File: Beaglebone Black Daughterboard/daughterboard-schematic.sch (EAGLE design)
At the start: 6 parts

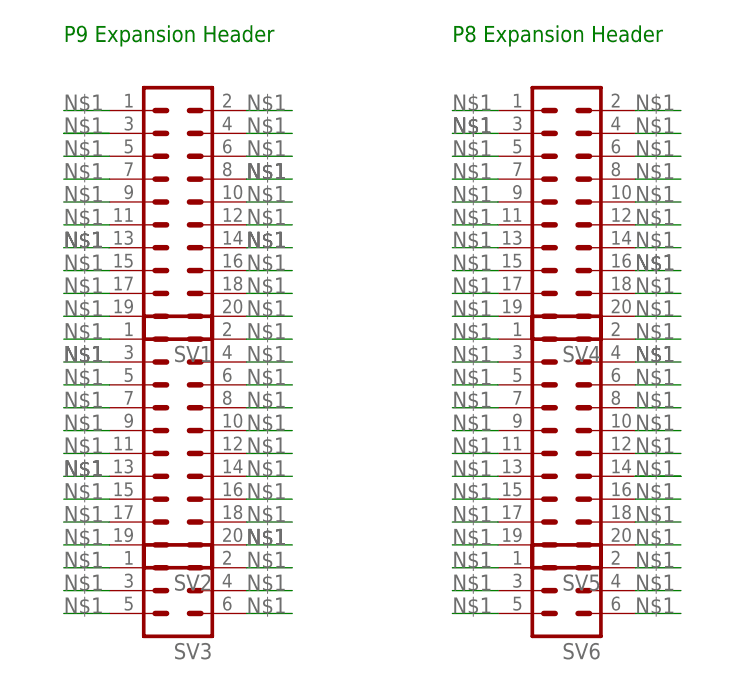
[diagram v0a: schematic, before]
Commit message: Label ports on Cape Expansion ready for wiring
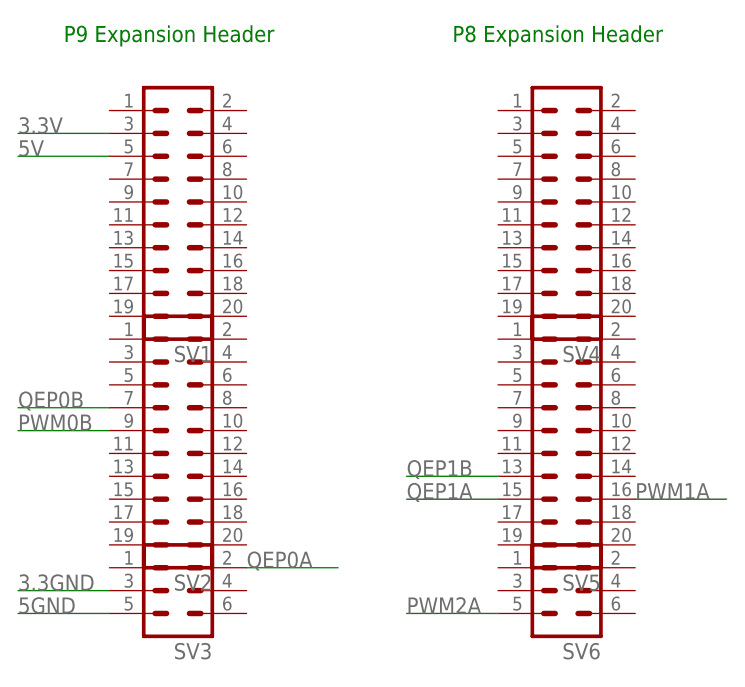
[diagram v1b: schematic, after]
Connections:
- net N$1 renamed 5V
- new net 3.3GND: SV3.3
- new net 3.3V: SV1.3
- new net 5GND: SV3.5
- new net PWM0B: SV2.9
- new net PWM1A: SV5.16
- new net PWM2A: SV6.5
- new net QEP0A: SV3.2
- new net QEP0B: SV2.7
- new net QEP1A: SV5.15
- new net QEP1B: SV5.13

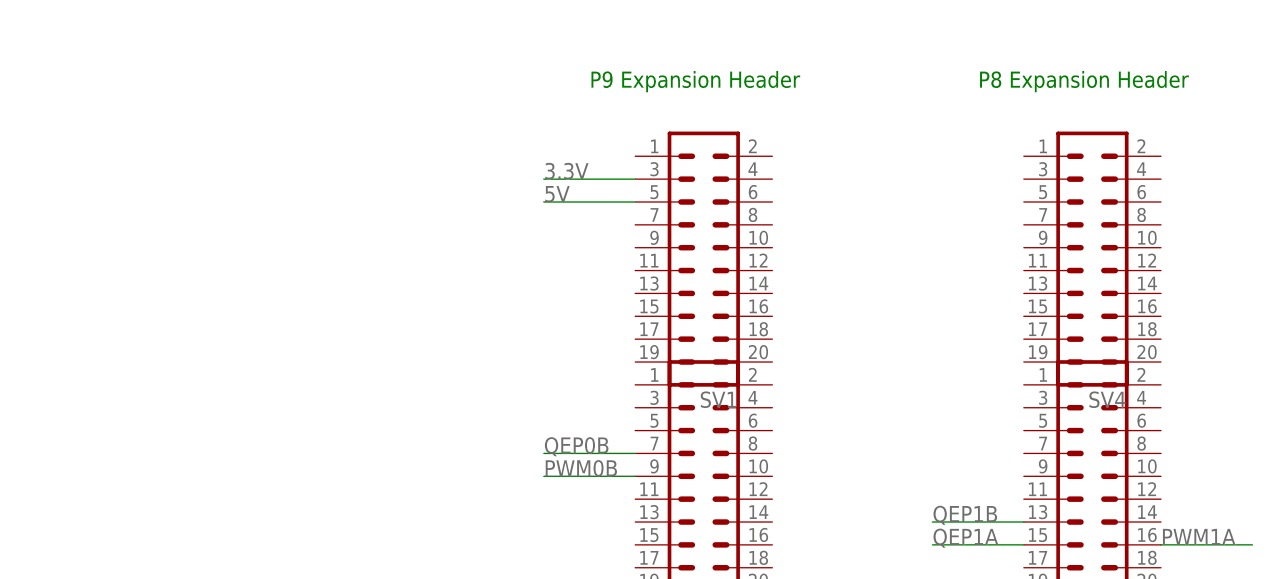
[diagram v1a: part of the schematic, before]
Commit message: Add pin holes for MPU6050
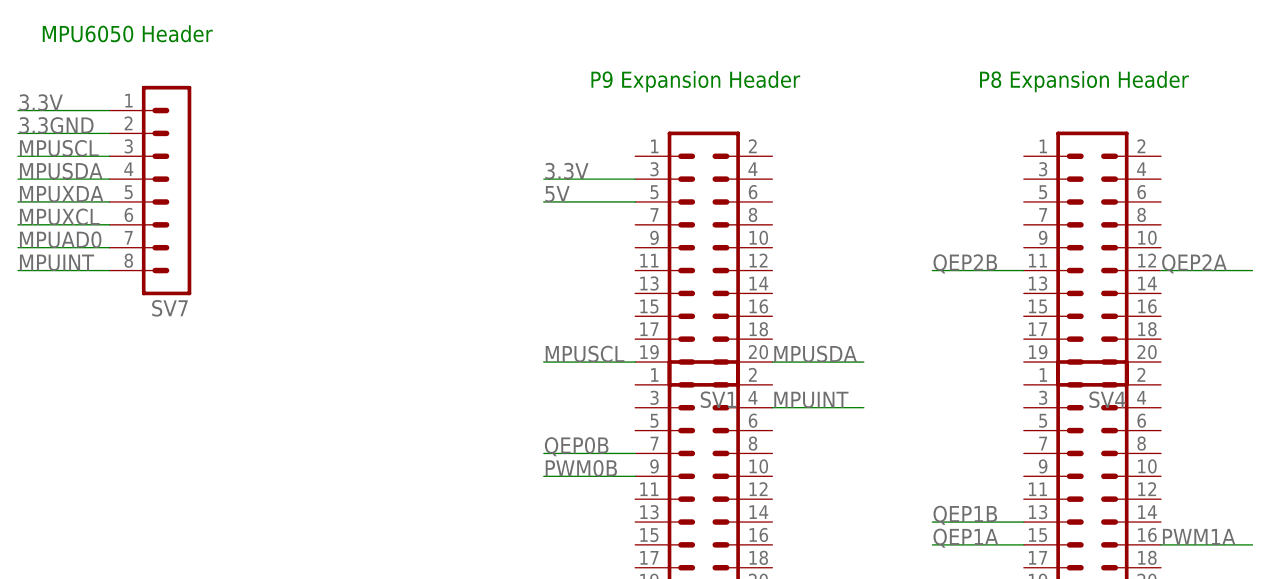
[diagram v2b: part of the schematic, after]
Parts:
- added SV7: (no value), con-lstb:MA08-1
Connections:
- new net MPUAD0: SV7.7
- new net MPUINT: SV2.4, SV7.8
- new net MPUSCL: SV1.19, SV7.3
- new net MPUSDA: SV1.20, SV7.4
- new net MPUXCL: SV7.6
- new net MPUXDA: SV7.5
- new net QEP2A: SV4.12
- new net QEP2B: SV4.11
- net 3.3GND: now also SV7.2
- net 3.3V: now also SV7.1
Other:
- note added: "MPU6050 Header"
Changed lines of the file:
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@@
 <part name="SV5" library="con-lstb" deviceset="MA10-2W" device=""/>
 <part name="SV6" library="con-lstb" deviceset="MA03-2" device=""/>
+<part name="SV7" library="con-lstb" deviceset="MA08-1" device=""/>
 </parts>
 <sheets>
@@
 <text x="134.62" y="104.14" size="1.778" layer="91">P9 Expansion Header</text>
 <text x="177.8" y="104.14" size="1.778" layer="91">P8 Expansion Header</text>
+<text x="73.66" y="109.22" size="1.778" layer="91">MPU6050 Header</text>
 </plain>
 <instances>
@@
 <instance part="SV5" gate="1" x="190.5" y="60.96" rot="R180"/>
 <instance part="SV6" gate="1" x="190.5" y="43.18" rot="R180"/>
+<instance part="SV7" gate="1" x="88.9" y="93.98" rot="R180"/>
 </instances>
 <busses>
@@
 <wire x1="139.7" y1="93.98" x2="129.54" y2="93.98" width="0.1524" layer="91"/>
 <label x="129.54" y="93.98" size="1.778" layer="95"/>
+</segment>
+<segment>
+<pinref part="SV7" gate="1" pin="1"/>
+<wire x1="81.28" y1="101.6" x2="71.12" y2="101.6" width="0.1524" layer="91"/>
+<label x="71.12" y="101.6" size="1.778" layer="95"/>
 </segment>
 </net>
@@
 <wire x1="139.7" y1="43.18" x2="129.54" y2="43.18" width="0.1524" layer="91"/>
 <label x="129.54" y="43.18" size="1.778" layer="95"/>
+</segment>
+<segment>
+<pinref part="SV7" gate="1" pin="2"/>
+<wire x1="81.28" y1="99.06" x2="71.12" y2="99.06" width="0.1524" layer="91"/>
+<label x="71.12" y="99.06" size="1.778" layer="95"/>
 </segment>
 </net>
@@
 </segment>
 </net>
+<net name="QEP2A" class="0">
+<segment>
+<pinref part="SV4" gate="1" pin="12"/>
+<wire x1="198.12" y1="83.82" x2="208.28" y2="83.82" width="0.1524" layer="91"/>
+<label x="198.12" y="83.82" size="1.778" layer="95"/>
+</segment>
+</net>
+<net name="QEP2B" class="0">
+<segment>
+<pinref part="SV4" gate="1" pin="11"/>
+<wire x1="182.88" y1="83.82" x2="172.72" y2="83.82" width="0.1524" layer="91"/>
+<label x="172.72" y="83.82" size="1.778" layer="95"/>
+</segment>
+</net>
+<net name="MPUSCL" class="0">
+<segment>
+<pinref part="SV1" gate="1" pin="19"/>
+<wire x1="139.7" y1="73.66" x2="129.54" y2="73.66" width="0.1524" layer="91"/>
+<label x="129.54" y="73.66" size="1.778" layer="95"/>
+</segment>
+<segment>
+<pinref part="SV7" gate="1" pin="3"/>
+<wire x1="81.28" y1="96.52" x2="71.12" y2="96.52" width="0.1524" layer="91"/>
+<label x="71.12" y="96.52" size="1.778" layer="95"/>
+</segment>
+</net>
+<net name="MPUSDA" class="0">
+<segment>
+<pinref part="SV1" gate="1" pin="20"/>
+<wire x1="154.94" y1="73.66" x2="165.1" y2="73.66" width="0.1524" layer="91"/>
+<label x="154.94" y="73.66" size="1.778" layer="95"/>
+</segment>
+<segment>
+<pinref part="SV7" gate="1" pin="4"/>
+<wire x1="81.28" y1="93.98" x2="71.12" y2="93.98" width="0.1524" layer="91"/>
+<label x="71.12" y="93.98" size="1.778" layer="95"/>
+</segment>
+</net>
+<net name="MPUINT" class="0">
+<segment>
+<pinref part="SV2" gate="1" pin="4"/>
+<wire x1="154.94" y1="68.58" x2="165.1" y2="68.58" width="0.1524" layer="91"/>
+<label x="154.94" y="68.58" size="1.778" layer="95"/>
+</segment>
+<segment>
+<pinref part="SV7" gate="1" pin="8"/>
+<wire x1="81.28" y1="83.82" x2="71.12" y2="83.82" width="0.1524" layer="91"/>
+<label x="71.12" y="83.82" size="1.778" layer="95"/>
+</segment>
+</net>
+<net name="MPUXDA" class="0">
+<segment>
+<pinref part="SV7" gate="1" pin="5"/>
+<wire x1="81.28" y1="91.44" x2="71.12" y2="91.44" width="0.1524" layer="91"/>
+<label x="71.12" y="91.44" size="1.778" layer="95"/>
+</segment>
+</net>
+<net name="MPUXCL" class="0">
+<segment>
+<pinref part="SV7" gate="1" pin="6"/>
+<wire x1="81.28" y1="88.9" x2="71.12" y2="88.9" width="0.1524" layer="91"/>
+<label x="71.12" y="88.9" size="1.778" layer="95"/>
+</segment>
+</net>
+<net name="MPUAD0" class="0">
+<segment>
+<pinref part="SV7" gate="1" pin="7"/>
+<wire x1="81.28" y1="86.36" x2="71.12" y2="86.36" width="0.1524" layer="91"/>
+<label x="71.12" y="86.36" size="1.778" layer="95"/>
+</segment>
+</net>
